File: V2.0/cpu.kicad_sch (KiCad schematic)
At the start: 14 parts, among them J2 Micro_SD_Card_Det1, U6 Pico W

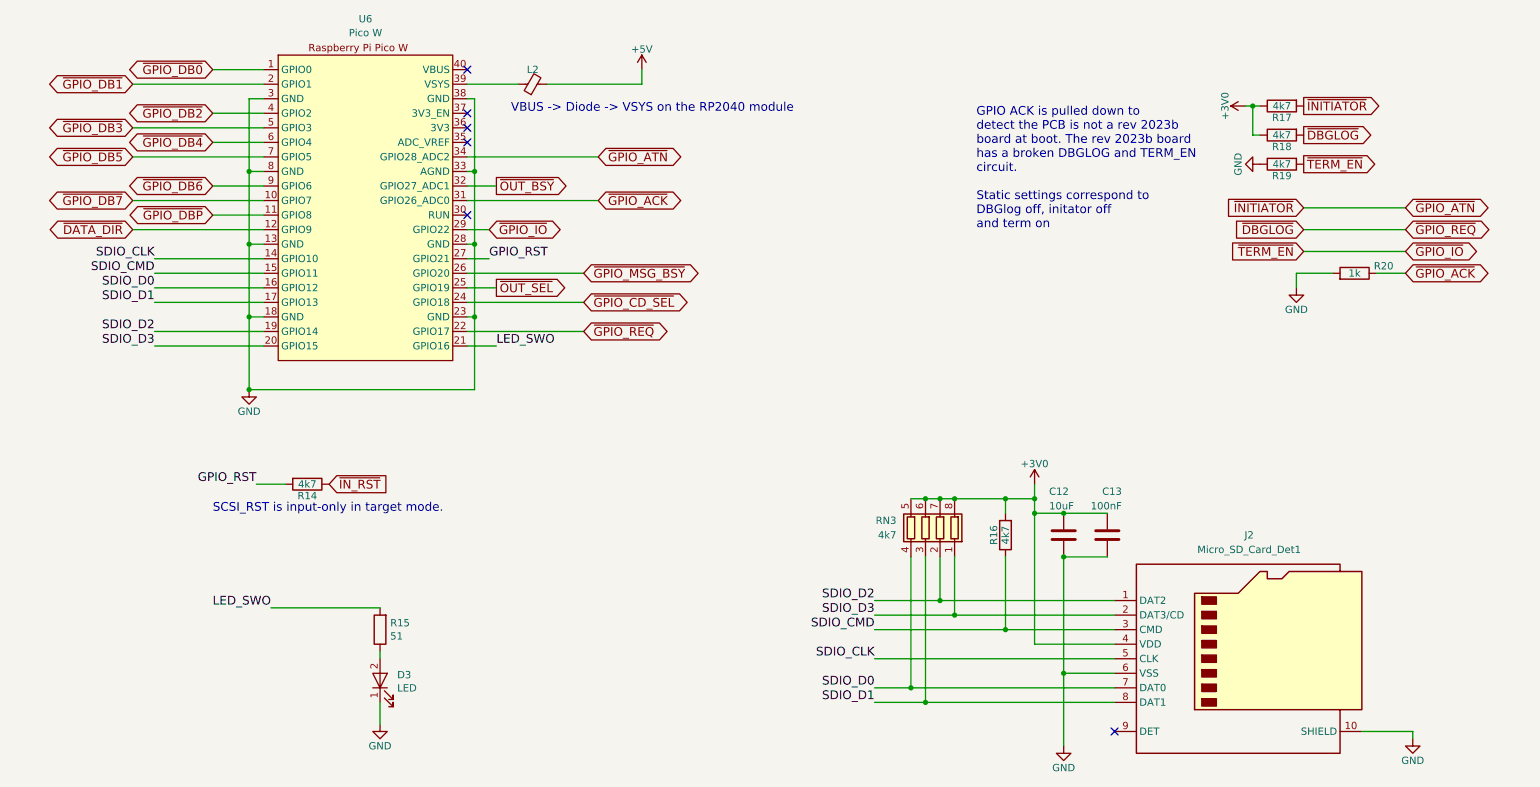
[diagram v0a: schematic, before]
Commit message: optimizations to buffers
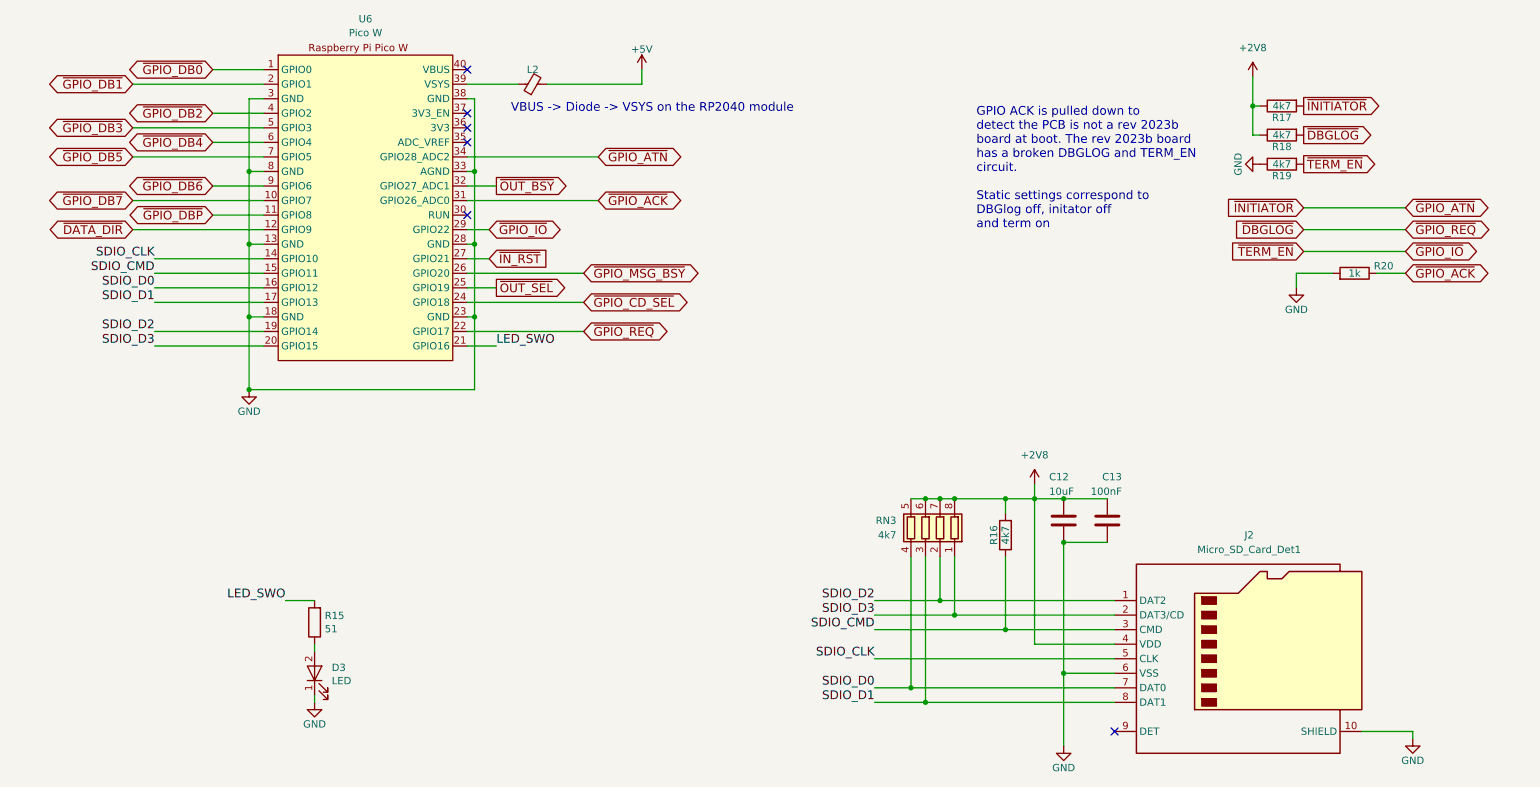
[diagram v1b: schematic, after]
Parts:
- removed R14: 4k7, Resistor_SMD:R_0603_1608Metric, symbol zuluscsi-rescue:R
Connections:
- net GPIO_RST is gone; now on net ~{IN_RST}: U6.27 (GPIO21)
- net +3V0 renamed +2V8
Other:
- note removed: "SCSI_RST is input-only in target mode."
- company: (C) Rabbit Hole Computing  -> ZZJ / M.D.
- title: ZuluSCSI (TM) Pico OSHW -> SillyTinySCSI
- moved on the sheet: C12, C13, D3, R15

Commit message: reverted some nuffer changes
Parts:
- R15: digikey (none) -> RMCF0603FT51R0TR-ND - Tape & Reel (TR)
- R17, R18, R19: LCSC (none) -> C23162; Manufacturer (none) -> Yageo; PartNumber (none) -> RC0603JR-074K7L; digikey (none) -> 311-100KHRTR-ND
- RN3: digikey YC164J-4.7KCT-ND -> RMCF0603FT51R0DKR-ND - Digi-Reel®
- U6: DIgikey 2648-SC0918CT-ND -> (none); digikey (none) -> 2648-SC0918CT-ND
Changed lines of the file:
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@@
       (effects (font (size 1.27 1.27)) hide)
     )
-    (property "digikey" "" (at 71.12 124.46 0)
+    (property "digikey" "RMCF0603FT51R0TR-ND - Tape & Reel (TR)" (at 71.12 124.46 0)
       (effects (font (size 1.27 1.27)) hide)
     )
@@
       (effects (font (size 1.27 1.27)) hide)
     )
-    (property "DIgikey" "2648-SC0918CT-ND " (at 80.01 52.07 0)
+    (property "DIgikey" "" (at 80.01 52.07 0)
       (effects (font (size 1.524 1.524)) hide)
+    )
+    (property "digikey" "2648-SC0918CT-ND " (at 80.01 52.07 0)
+      (effects (font (size 1.27 1.27)) hide)
     )
     (pin "1")
@@
       (effects (font (size 1.27 1.27)) hide)
     )
-    (property "digikey" "YC164J-4.7KCT-ND" (at 177.8 107.95 0)
+    (property "digikey" "RMCF0603FT51R0DKR-ND - Digi-Reel®" (at 177.8 107.95 0)
       (effects (font (size 1.27 1.27)) hide)
     )
@@
       (effects (font (size 1.27 1.27)))
     )
-    (property "LCSC" "" (at 240.03 44.45 0)
-      (effects (font (size 1.27 1.27)) hide)
-    )
-    (property "Manufacturer" "" (at 240.03 44.45 0)
-      (effects (font (size 1.27 1.27)) hide)
-    )
-    (property "PartNumber" "" (at 240.03 44.45 0)
-      (effects (font (size 1.27 1.27)) hide)
-    )
-    (property "digikey" "" (at 240.03 44.45 0)
+    (property "LCSC" "C23162" (at 240.03 44.45 0)
+      (effects (font (size 1.27 1.27)) hide)
+    )
+    (property "Manufacturer" "Yageo" (at 240.03 44.45 0)
+      (effects (font (size 1.27 1.27)) hide)
+    )
+    (property "PartNumber" "RC0603JR-074K7L" (at 240.03 44.45 0)
+      (effects (font (size 1.27 1.27)) hide)
+    )
+    (property "digikey" "311-100KHRTR-ND" (at 240.03 44.45 0)
       (effects (font (size 1.27 1.27)) hide)
     )
@@
       (effects (font (size 1.27 1.27)))
     )
-    (property "LCSC" "" (at 240.03 34.29 0)
-      (effects (font (size 1.27 1.27)) hide)
-    )
-    (property "Manufacturer" "" (at 240.03 34.29 0)
-      (effects (font (size 1.27 1.27)) hide)
-    )
-    (property "PartNumber" "" (at 240.03 34.29 0)
-      (effects (font (size 1.27 1.27)) hide)
-    )
-    (property "digikey" "" (at 240.03 34.29 0)
+    (property "LCSC" "C23162" (at 240.03 34.29 0)
+      (effects (font (size 1.27 1.27)) hide)
+    )
+    (property "Manufacturer" "Yageo" (at 240.03 34.29 0)
+      (effects (font (size 1.27 1.27)) hide)
+    )
+    (property "PartNumber" "RC0603JR-074K7L" (at 240.03 34.29 0)
+      (effects (font (size 1.27 1.27)) hide)
+    )
+    (property "digikey" "311-100KHRTR-ND" (at 240.03 34.29 0)
       (effects (font (size 1.27 1.27)) hide)
     )
@@
       (effects (font (size 1.27 1.27)))
     )
-    (property "LCSC" "" (at 240.03 39.37 0)
-      (effects (font (size 1.27 1.27)) hide)
-    )
-    (property "Manufacturer" "" (at 240.03 39.37 0)
-      (effects (font (size 1.27 1.27)) hide)
-    )
-    (property "PartNumber" "" (at 240.03 39.37 0)
-      (effects (font (size 1.27 1.27)) hide)
-    )
-    (property "digikey" "" (at 240.03 39.37 0)
-      (effects (font (size 1.27 1.27)) hide)
-    )
+    (property "LCSC" "C23162" (at 240.03 39.37 0)
+      (effects (font (size 1.27 1.27)) hide)
+    )
+    (property "Manufacturer" "Yageo" (at 240.03 39.37 0)
+      (effects (font (size 1.27 1.27)) hide)
+    )
+    (property "PartNumber" "RC0603JR-074K7L" (at 240.03 39.37 0)
+      (effects (font (size 1.27 1.27)) hide)
+    )
+    (property "digikey" "311-100KHRTR-ND" (at 240.03 39.37 0)
+      (effects (font (size 1.27 1.27)) hide)
+    )

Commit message: last resistor pack
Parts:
- D3: JLCPCB_IGNORE do not fit -> (none); LCSC n/a -> C84256; Manufacturer Osram Opto Semiconductors Inc -> Harvatek Corporation; PartNumber HSMC-C170-T0000 -> B1701UD--20D000414U1930
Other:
- moved on the sheet: D3, R15
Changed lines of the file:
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@@
     (stroke (width 0) (type default))
   )
-  (wire (pts (xy 66.04 120.65) (xy 71.12 120.65))
+  (wire (pts (xy 85.09 107.95) (xy 90.17 107.95))
     (stroke (width 0) (type default))
   )
@@
     (stroke (width 0) (type default))
   )
-  (wire (pts (xy 71.12 129.54) (xy 71.12 128.27))
+  (wire (pts (xy 90.17 116.84) (xy 90.17 115.57))
     (stroke (width 0) (type default))
   )
@@
     (stroke (width 0) (type default))
   )
-  (wire (pts (xy 71.12 137.16) (xy 71.12 138.43))
+  (wire (pts (xy 90.17 124.46) (xy 90.17 125.73))
     (stroke (width 0) (type default))
   )
@@
     (effects (font (size 1.524 1.524)) (justify right bottom))
   )
-  (label "LED_SWO" (at 66.04 120.65 180) (fields_autoplaced)
+  (label "LED_SWO" (at 85.09 107.95 180) (fields_autoplaced)
     (effects (font (size 1.524 1.524)) (justify right bottom))
   )
@@
     )
   )
-  (symbol (lib_id "zuluscsi-rescue:LED") (at 71.12 133.35 90) (unit 1)
+  (symbol (lib_id "zuluscsi-rescue:LED") (at 90.17 120.65 90) (unit 1)
     (in_bom yes) (on_board yes) (dnp no)
-    (property "Reference" "D3" (at 74.1172 132.3594 90)
+    (property "Reference" "D3" (at 93.1672 119.6594 90)
       (effects (font (size 1.27 1.27)) (justify right))
     )
-    (property "Value" "LED" (at 74.1172 134.6708 90)
+    (property "Value" "LED" (at 93.1672 121.9708 90)
       (effects (font (size 1.27 1.27)) (justify right))
     )
-    (property "Footprint" "LED_SMD:LED_0805_2012Metric" (at 71.12 133.35 0)
-      (effects (font (size 1.27 1.27)) hide)
-    )
-    (property "Datasheet" "" (at 71.12 133.35 0)
-      (effects (font (size 1.27 1.27)))
-    )
-    (property "LCSC" "n/a" (at 71.12 133.35 0)
-      (effects (font (size 1.27 1.27)) hide)
-    )
-    (property "Manufacturer" "Osram Opto Semiconductors Inc" (at 71.12 133.35 0)
-      (effects (font (size 1.27 1.27)) hide)
-    )
-    (property "PartNumber" "HSMC-C170-T0000" (at 71.12 133.35 0)
-      (effects (font (size 1.27 1.27)) hide)
-    )
-    (property "digikey" "3147-B1701UD--20D000414U1930CT-ND" (at 71.12 133.35 0)
-      (effects (font (size 1.27 1.27)) hide)
-    )
-    (property "JLCPCBCORRECT" "" (at 71.12 133.35 0)
-      (effects (font (size 1.27 1.27)) hide)
-    )
-    (property "JLCPCB_IGNORE" "do not fit" (at 71.12 133.35 0)
+    (property "Footprint" "LED_SMD:LED_0805_2012Metric" (at 90.17 120.65 0)
+      (effects (font (size 1.27 1.27)) hide)
+    )
+    (property "Datasheet" "" (at 90.17 120.65 0)
+      (effects (font (size 1.27 1.27)))
+    )
+    (property "LCSC" "C84256" (at 90.17 120.65 0)
+      (effects (font (size 1.27 1.27)) hide)
+    )
+    (property "Manufacturer" "Harvatek Corporation" (at 90.17 120.65 0)
+      (effects (font (size 1.27 1.27)) hide)
+    )
+    (property "PartNumber" "B1701UD--20D000414U1930" (at 90.17 120.65 0)
+      (effects (font (size 1.27 1.27)) hide)
+    )
+    (property "digikey" "3147-B1701UD--20D000414U1930CT-ND" (at 90.17 120.65 0)
+      (effects (font (size 1.27 1.27)) hide)
+    )
+    (property "JLCPCBCORRECT" "" (at 90.17 120.65 0)
+      (effects (font (size 1.27 1.27)) hide)
+    )
+    (property "JLCPCB_IGNORE" "" (at 90.17 120.65 0)
       (effects (font (size 1.27 1.27)) hide)
     )
@@
     )
   )
-  (symbol (lib_id "zuluscsi-rescue:R") (at 71.12 124.46 180) (unit 1)
+  (symbol (lib_id "zuluscsi-rescue:R") (at 90.17 111.76 180) (unit 1)
     (in_bom yes) (on_board yes) (dnp no)
-    (property "Reference" "R15" (at 72.898 123.2916 0)
+    (property "Reference" "R15" (at 91.948 110.5916 0)
       (effects (font (size 1.27 1.27)) (justify right))
     )
-    (property "Value" "51" (at 72.898 125.603 0)
+    (property "Value" "51" (at 91.948 112.903 0)
       (effects (font (size 1.27 1.27)) (justify right))
     )
-    (property "Footprint" "Resistor_SMD:R_0603_1608Metric" (at 72.898 124.46 90)
-      (effects (font (size 1.27 1.27)) hide)
-    )
-    (property "Datasheet" "" (at 71.12 124.46 0)
-      (effects (font (size 1.27 1.27)))
-    )
-    (property "LCSC" "C23197" (at 71.12 124.46 0)
-      (effects (font (size 1.27 1.27)) hide)
-    )
-    (property "Manufacturer" "Yageo" (at 71.12 124.46 0)
-      (effects (font (size 1.27 1.27)) hide)
-    )
-    (property "PartNumber" "0603WAF510JT5E" (at 71.12 124.46 0)
-      (effects (font (size 1.27 1.27)) hide)
-    )
-    (property "digikey" "RMCF0603FT51R0TR-ND - Tape & Reel (TR)" (at 71.12 124.46 0)
-      (effects (font (size 1.27 1.27)) hide)
-    )
-    (property "JLCPCBCORRECT" "" (at 71.12 124.46 0)
-      (effects (font (size 1.27 1.27)) hide)
-    )
-    (property "JLCPCB_IGNORE" "" (at 71.12 124.46 0)
+    (property "Footprint" "Resistor_SMD:R_0603_1608Metric" (at 91.948 111.76 90)
+      (effects (font (size 1.27 1.27)) hide)
+    )
+    (property "Datasheet" "" (at 90.17 111.76 0)
+      (effects (font (size 1.27 1.27)))
+    )
+    (property "LCSC" "C23197" (at 90.17 111.76 0)
+      (effects (font (size 1.27 1.27)) hide)
+    )
+    (property "Manufacturer" "Yageo" (at 90.17 111.76 0)
+      (effects (font (size 1.27 1.27)) hide)
+    )
+    (property "PartNumber" "0603WAF510JT5E" (at 90.17 111.76 0)
+      (effects (font (size 1.27 1.27)) hide)
+    )
+    (property "digikey" "RMCF0603FT51R0TR-ND - Tape & Reel (TR)" (at 90.17 111.76 0)
+      (effects (font (size 1.27 1.27)) hide)
+    )
+    (property "JLCPCBCORRECT" "" (at 90.17 111.76 0)
+      (effects (font (size 1.27 1.27)) hide)
+    )
+    (property "JLCPCB_IGNORE" "" (at 90.17 111.76 0)
       (effects (font (size 1.27 1.27)) hide)
     )
@@
     )
   )
-  (symbol (lib_id "zuluscsi-rescue:GND") (at 71.12 138.43 0) (unit 1)
+  (symbol (lib_id "zuluscsi-rescue:GND") (at 90.17 125.73 0) (unit 1)
     (in_bom yes) (on_board yes) (dnp no)
-    (property "Reference" "#PWR036" (at 71.12 144.78 0)
-      (effects (font (size 1.27 1.27)) hide)
-    )
-    (property "Value" "GND" (at 71.12 142.24 0)
-      (effects (font (size 1.27 1.27)))
-    )
-    (property "Footprint" "" (at 71.12 138.43 0)
-      (effects (font (size 1.27 1.27)))
-    )
-    (property "Datasheet" "" (at 71.12 138.43 0)
-      (effects (font (size 1.27 1.27)))
-    )
+    (property "Reference" "#PWR036" (at 90.17 132.08 0)
+      (effects (font (size 1.27 1.27)) hide)
+    )
+    (property "Value" "GND" (at 90.17 129.54 0)
+      (effects (font (size 1.27 1.27)))
+    )
+    (property "Footprint" "" (at 90.17 125.73 0)
+      (effects (font (size 1.27 1.27)))
+    )
+    (property "Datasheet" "" (at 90.17 125.73 0)
+      (effects (font (size 1.27 1.27)))
+    )

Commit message: pwr routed
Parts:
- removed L2: Ferrite_Bead_Small, Inductor_SMD:L_0603_1608Metric, symbol Device:FerriteBead_Small
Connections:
- net 5V_IN: now reaches U6.39 (VSYS)
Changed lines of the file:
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@@
-    (stroke (width 0) (type default))
-  )
-  (wire (pts (xy 128.27 30.48) (xy 128.27 27.94))
     (stroke (width 0) (type default))
   )
@@
   )
   (wire (pts (xy 180.34 113.03) (xy 180.34 120.65))
-    (stroke (width 0) (type default))
-  )
-  (wire (pts (xy 111.76 30.48) (xy 128.27 30.48))
     (stroke (width 0) (type default))
   )
@@
     (property "Intersheetrefs" "${INTERSHEET_REFS}" (at 185.42 -101.6 0)
       (effects (font (size 1.27 1.27)) hide)
+    )
+  )
+  (global_label "5V_IN" (shape output) (at 106.68 30.48 0) (fields_autoplaced)
+    (effects (font (size 1.524 1.524)) (justify left))
+    (property "Intersheetrefs" "${INTERSHEET_REFS}" (at 115.7179 30.48 0)
+      (effects (font (size 1.27 1.27)) (justify left) hide)
     )
   )
@@
     )
   )
-  (symbol (lib_id "zuluscsi-rescue:+5V") (at 128.27 27.94 0) (unit 1)
-    (in_bom yes) (on_board yes) (dnp no)
-    (property "Reference" "#PWR063" (at 128.27 31.75 0)
-      (effects (font (size 1.27 1.27)) hide)
-    )
-    (property "Value" "+5V" (at 128.27 24.384 0)
-      (effects (font (size 1.27 1.27)))
-    )
-    (property "Footprint" "" (at 128.27 27.94 0)
-      (effects (font (size 1.524 1.524)))
-    )
-    (property "Datasheet" "" (at 128.27 27.94 0)
-      (effects (font (size 1.524 1.524)))
-    )
-    (pin "1")
-    (instances
-      (project "SillyTinySCSI"
-        (path "/0a1a4d88-972a-46ce-b25e-6cb796bd41f7/00000000-0000-0000-0000-000055ff7b90"
-          (reference "#PWR063") (unit 1)
-        )
-        (path "/0a1a4d88-972a-46ce-b25e-6cb796bd41f7/00000000-0000-0000-0000-000055ff7cc4"
-          (reference "#PWR037") (unit 1)
-        )
-      )
-    )
-  )
   (symbol (lib_id "zuluscsi-rescue:R") (at 191.77 109.22 180) (unit 1)
     (in_bom yes) (on_board yes) (dnp no)
@@
         )
       )
-    )
-  )
-  (symbol (lib_id "Device:FerriteBead_Small") (at 109.22 30.48 90) (unit 1)
-    (in_bom yes) (on_board yes) (dnp no)
-    (property "Reference" "L2" (at 109.22 27.94 90)
-      (effects (font (size 1.27 1.27)))
-    )
-    (property "Value" "Ferrite_Bead_Small" (at 110.363 27.94 0)
-      (effects (font (size 1.27 1.27)) (justify left) hide)
-    )
-    (property "Footprint" "Inductor_SMD:L_0603_1608Metric" (at 109.22 32.258 90)
-      (effects (font (size 1.27 1.27)) hide)
-    )
-    (property "Datasheet" "~" (at 109.22 30.48 0)
-      (effects (font (size 1.27 1.27)) hide)
-    )
-    (property "LCSC" "C1002" (at 109.22 30.48 0)
-      (effects (font (size 1.27 1.27)) hide)
-    )
-    (property "Manufacturer" "Pulse Electronics Network" (at 109.22 30.48 0)
-      (effects (font (size 1.27 1.27)) hide)
-    )
-    (property "PartNumber" "PE-0603FB601ST" (at 109.22 30.48 0)
-      (effects (font (size 1.27 1.27)) hide)
-    )
-    (property "digikey" "553-2384-2-ND" (at 109.22 30.48 0)
-      (effects (font (size 1.27 1.27)) hide)
-    )
-    (property "JLCPCBCORRECT" "" (at 109.22 30.48 0)
-      (effects (font (size 1.27 1.27)) hide)
-    )
-    (property "JLCPCB_IGNORE" "" (at 109.22 30.48 0)
-      (effects (font (size 1.27 1.27)) hide)
-    )
-    (pin "1")
-    (pin "2")
-    (instances
-      (project "SillyTinySCSI"
-        (path "/0a1a4d88-972a-46ce-b25e-6cb796bd41f7/00000000-0000-0000-0000-000055ff7cc4"
-          (reference "L2") (unit 1)
-        )
-      )

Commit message: sync up
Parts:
- removed RN3: 4k7, Resistor_SMD:R_Array_Convex_4x0603, symbol Device:R_Pack04
- added R32, R33, R34, R35: 4k7, Resistor_SMD:R_0603_1608Metric, symbol zuluscsi-rescue:R
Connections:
- net +2V8: now also R32.2, R33.2, R34.2, R35.2
- net SDIO_D0: now also R35.1
- net SDIO_D1: now also R34.1
- net SDIO_D2: now also R33.1
- net SDIO_D3: now also R32.1
- net 5V_IN renamed +5VP
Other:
- note added: "VBUS -> Diode -> VSYS on the RP2040 module Pico has plenty of onboard capacitance"
- note removed: "VBUS -> Diode -> VSYS on the RP2040 module"

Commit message: bring current
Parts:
- added R36: 4k7, Resistor_SMD:R_0603_1608Metric, symbol zuluscsi-rescue:R
- added U1: 74LVT125, ZuluSCSI:SSOP_TSSOP-14_4.4x5mm_Pitch0.65mm_PCBWay-MaskClearance0.22mm, symbol 74xx:74LVC125
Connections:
- net GND: now also U1.10
- net LED_SWO: now also U1.9; no longer R15.2
- net ~{IN_RST}: now also R36.2; no longer U6.27 (GPIO21)
- new net: R15.2, U1.8
- new net: R36.1, U6.27 (GPIO21)
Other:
- note added: "buffer for increased output current (otherwise unused buffer)"
- note added: "resistor maintain HW compatibility with Zulu pico which may switch GP21 temporarily to output"
- moved on the sheet: D3, R15
